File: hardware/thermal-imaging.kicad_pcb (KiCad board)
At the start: 2 copper layers, 40 x 40 mm, 39 parts, among them P1 CON-SENSOR, P2 Boot, Q1 Oscillator, U1 XMC1XXX24, U10 DRILL, U11 DRILL, U2 74LVC1G17, U3 74LVC1G17, U4 FLIR-Lepton, U5 AP7333-28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

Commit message: routing completed
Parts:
- added Fiducial_Mark: VAL**, kicad-libraries:Fiducial_Mark, F.Cu at (200.4, 114.9)
- added Fiducial_Mark: VAL**, kicad-libraries:Fiducial_Mark, F.Cu at (174.4, 118.9)
- added Fiducial_Mark: VAL**, kicad-libraries:Fiducial_Mark, F.Cu at (176.4, 84.9)
- added Fiducial_Mark: VAL**, kicad-libraries:Fiducial_Mark, F.Cu at (199.4, 82.9)
- added G***: Logo_31x31, kicad-libraries:Logo_31x31, F.Cu at (193.4, 114.6)
- added G***: LOGO, kicad-libraries:Logo_CoMCU, B.Cu at (186.4, 100.9)
- added G***: LOGO, kicad-libraries:WEEE_7mm, B.Cu at (194.4, 100.9)
- added VAL: CE_5mm, kicad-libraries:CE_5mm, B.Cu at (178.4, 100.9)
- moved FB1 2.80 mm to (196.2, 108.1)
- moved C1 1.60 mm to (198.4, 107.3), turned to 180 degrees
- moved C2 1.60 mm to (198.4, 108.9), turned to 180 degrees
- moved C12 1.41 mm to (172.3, 99.9)
- moved Q1 1.30 mm to (174.9, 99.9)
- moved R4 1.20 mm to (178.5, 98.6)
- moved C3 1.00 mm to (196.5, 82.4)
- moved U1 0.80 mm to (196.5, 86.3)
- moved RP1 0.22 mm to (200.9, 89.1)
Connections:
- U1 pad 16: (no net) -> RESET
- U1 pad 2: RESET -> (no net)
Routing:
- net 3V3: track 0.00 -> 116.1 mm, vias 0 -> 2
- net +2.8V: track 0.00 -> 96.9 mm, vias 0 -> 5
- net GND: track 0.00 -> 65.8 mm, vias 0 -> 42
- net RESET: track 0.00 -> 29.0 mm, vias 0 -> 6
- net SDA: track 0.00 -> 28.4 mm, vias 0 -> 6
- net VSYNC: track 0.00 -> 25.2 mm
- net SCL: track 0.00 -> 23.7 mm, vias 0 -> 4
- net M-MISO: track 0.00 -> 18.7 mm, vias 0 -> 2
- net +2.8V_INT: track 0.00 -> 16.9 mm, vias 0 -> 2
- net +1.2V_INT: track 0.00 -> 13.6 mm, vias 0 -> 2
- net Net-(RP3-Pad7): track 0.00 -> 10.4 mm
- net Net-(FILTER1-Pad1): track 0.00 -> 10.1 mm
- net Net-(C1-Pad2): track 0.00 -> 9.54 mm
- net Net-(FILTER1-Pad2): track 0.00 -> 8.47 mm
- net Net-(P2-Pad2): track 0.00 -> 8.39 mm
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- added copper zone on B.Cu, net GND
- added copper zone on F.Cu, net GND

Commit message: add description text
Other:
- board text added: "Copyright Tinkerforge GmbH 2017. This documentation describes Open Hardware and is licensed under the CERN OHL v. 1.1. You may redistribute and modify this documentation under the terms of the CERN OHL v.1.1. (http://ohwr.org/cernohl). This documentation is distributed WITHOUT ANY EXPRESS OR IMPLIED WARRANTY, INCLUDING OF MERCHANTABILITY, SATISFACTORY QUALITY AND FITNESS FOR A PARTICULAR PURPOSE.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"
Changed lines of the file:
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@@
     (links 151)
     (no_connects 0)
-    (area 166.324999 80.824999 206.475001 120.975001)
+    (area 165.544999 80.044999 207.255001 121.755001)
     (thickness 1.6)
-    (drawings 11)
+    (drawings 12)
     (tracks 522)
     (zones 0)
@@
   )
   (page A4)
+  (title_block
+    (title "Thermal Imaging Bricklet")
+    (date 2017-02-08)
+    (rev 1.0)
+    (company "Tinkerforge GmbH")
+    (comment 1 "Licensed under CERN OHL v.1.1")
+    (comment 2 "Copyright (©) 2017, B.Nordmeyer <bastian@tinkerforge.com>")
+  )
   (layers
     (0 F.Cu signal hide)
@@
   )
   (setup
-    (last_trace_width 0.3)
+    (last_trace_width 0.2)
     (user_trace_width 0.2)
     (user_trace_width 0.25)
@@
       (xy 2.48217 3.513666) (xy 2.482863 3.409859) (xy 2.482863 3.409859)) (layer B.SilkS) (width 0.1))
   )
+  (gr_text "Copyright Tinkerforge GmbH 2017.\nThis documentation describes Open Hardware and is licensed under the\nCERN OHL v. 1.1.\nYou may redistribute and modify this documentation under the terms of the\nCERN OHL v.1.1. (http://ohwr.org/cernohl). This documentation is distributed\nWITHOUT ANY EXPRESS OR IMPLIED WARRANTY, INCLUDING OF\nMERCHANTABILITY, SATISFACTORY QUALITY AND FITNESS FOR A\nPARTICULAR PURPOSE. Please see the CERN OHL v.1.1 for applicable\nconditions" (at 258.4 154.9) (layer Cmts.User)
+    (effects (font (size 0.8 0.8) (thickness 0.2)))
+  )
   (gr_text Status (at 186.4 82.6) (layer F.SilkS)

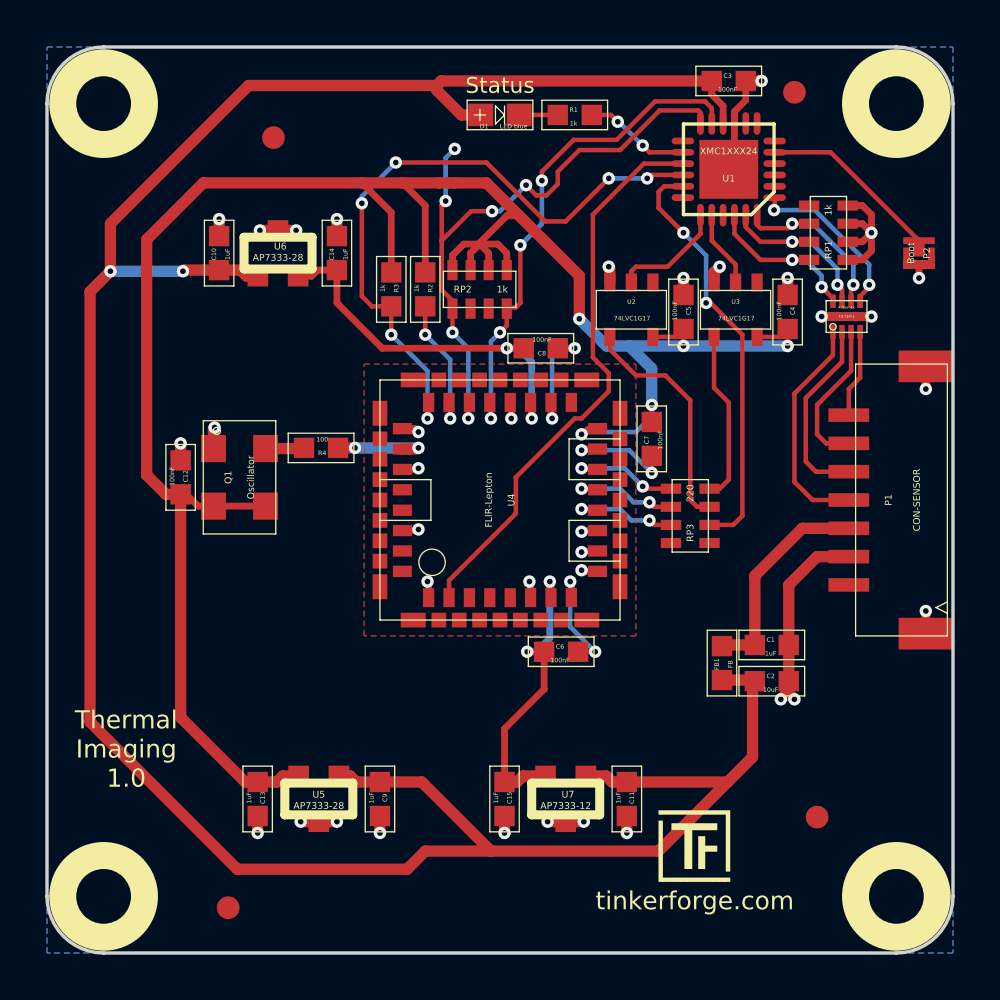
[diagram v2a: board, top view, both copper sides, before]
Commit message: fix wrong footprint
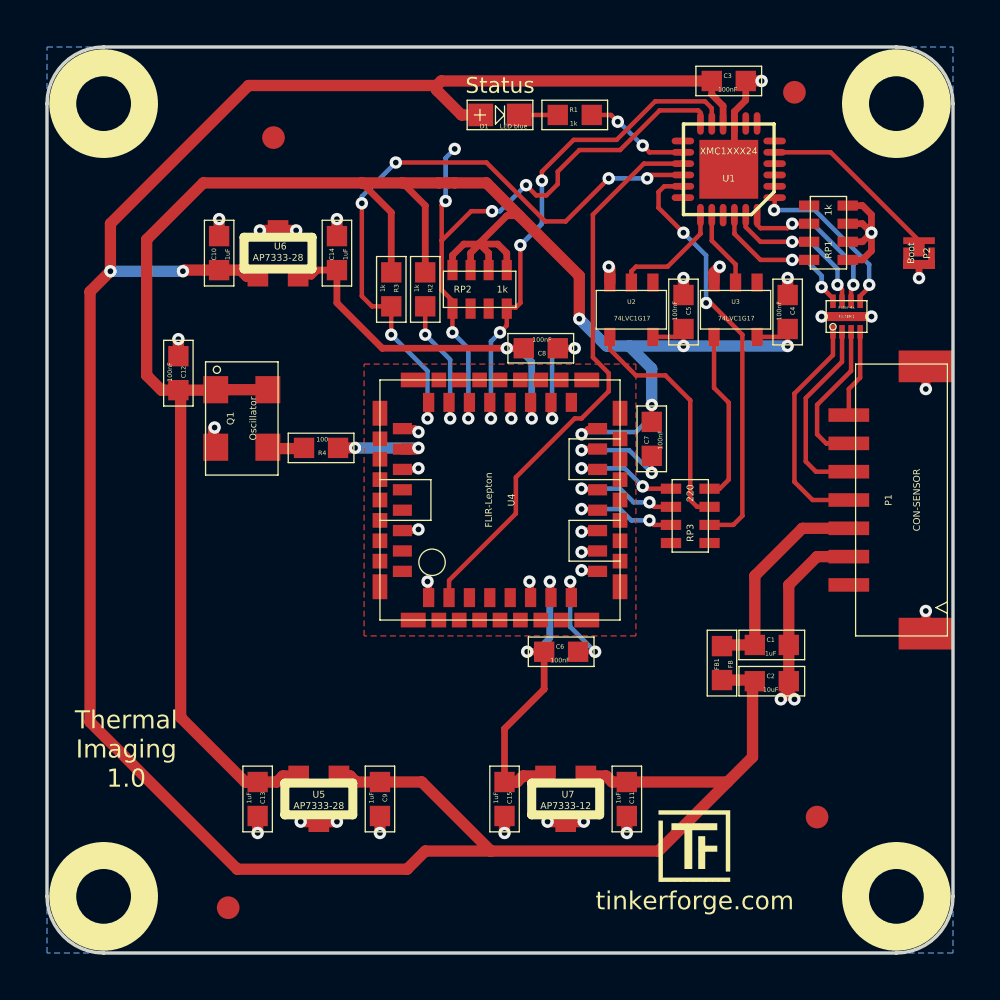
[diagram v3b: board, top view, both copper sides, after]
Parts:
- Q1: footprint CRYSTAL_5032 -> kicad-libraries:CRYSTAL_5032
- moved C12 4.60 mm to (172.2, 95.3)
- moved Q1 2.60 mm to (175.0, 97.3)
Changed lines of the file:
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@@
     (links 151)
     (no_connects 0)
-    (area 165.544999 80.044999 207.255001 121.755001)
+    (area 165.544999 80.044999 282.44286 160.84)
     (thickness 1.6)
     (drawings 12)
@@
   )
   (layers
-    (0 F.Cu signal hide)
+    (0 F.Cu signal)
     (31 B.Cu signal hide)
     (32 B.Adhes user hide)
@@
   )
   (setup
-    (last_trace_width 0.2)
+    (last_trace_width 0.5)
     (user_trace_width 0.2)
     (user_trace_width 0.25)
@@
   )
   (module kicad-libraries:0603F (layer F.Cu)
-    (at 172.3 99.9 90)
+    (at 172.2 95.3 90)
     (attr smd)
     (fp_text reference C12 (at 0.05 0.225 90) (layer F.SilkS)
@@
       (net 1 GND))
   )
-  (module CRYSTAL_5032 (layer F.Cu)
-    (at 174.9 99.9 270)
-    (fp_text reference Q1 (at 0 0.5 270) (layer F.SilkS)
-      (effects (font (size 0.3 0.3) (thickness 0.075)))
-    )
-    (fp_text value Oscillator (at 0 -0.5 270) (layer F.SilkS)
-      (effects (font (size 0.3 0.3) (thickness 0.075)))
-    )
-    (fp_circle (center -2.05 1) (end -2 1.15) (layer F.SilkS) (width 0.05))
-    (fp_line (start -2.5 -1.6) (end 2.5 -1.6) (layer F.SilkS) (width 0.05))
-    (fp_line (start 2.5 -1.6) (end 2.5 1.6) (layer F.SilkS) (width 0.05))
-    (fp_line (start 2.5 1.6) (end -2.5 1.6) (layer F.SilkS) (width 0.05))
-    (fp_line (start -2.5 1.6) (end -2.5 -1.6) (layer F.SilkS) (width 0.05))
-    (pad 1 smd rect (at 1.27 1.15 270) (size 1.2 1.1) (layers F.Cu F.Paste F.Mask)
-      (net 31 +2.8V))
-    (pad 2 smd rect (at -1.27 1.15 270) (size 1.2 1.1) (layers F.Cu F.Paste F.Mask)
-      (net 1 GND))
-    (pad 3 smd rect (at -1.27 -1.15 270) (size 1.2 1.1) (layers F.Cu F.Paste F.Mask)
-      (net 19 "Net-(Q1-Pad3)"))
-    (pad 4 smd rect (at 1.27 -1.15 270) (size 1.2 1.1) (layers F.Cu F.Paste F.Mask)
-      (net 31 +2.8V))
-  )
   (module 0603F (layer F.Cu)
     (at 189.7 83.9 180)
@@
       (xy 2.48217 3.513666) (xy 2.482863 3.409859) (xy 2.482863 3.409859)) (layer B.SilkS) (width 0.1))
   )
+  (module kicad-libraries:CRYSTAL_5032 (layer F.Cu)
+    (at 175 97.3 270)
+    (fp_text reference Q1 (at 0 0.5 270) (layer F.SilkS)
+      (effects (font (size 0.3 0.3) (thickness 0.075)))
+    )
+    (fp_text value Oscillator (at 0 -0.5 270) (layer F.SilkS)
+      (effects (font (size 0.3 0.3) (thickness 0.075)))
+    )
+    (fp_circle (center -2.15 1.1) (end -2.1 1.25) (layer F.SilkS) (width 0.05))
+    (fp_line (start -2.5 -1.6) (end 2.5 -1.6) (layer F.SilkS) (width 0.05))
+    (fp_line (start 2.5 -1.6) (end 2.5 1.6) (layer F.SilkS) (width 0.05))
+    (fp_line (start 2.5 1.6) (end -2.5 1.6) (layer F.SilkS) (width 0.05))
+    (fp_line (start -2.5 1.6) (end -2.5 -1.6) (layer F.SilkS) (width 0.05))
+    (pad 2 smd rect (at 1.27 1.15 270) (size 1.2 1.1) (layers F.Cu F.Paste F.Mask)
+      (net 1 GND))
+    (pad 1 smd rect (at -1.27 1.15 270) (size 1.2 1.1) (layers F.Cu F.Paste F.Mask)
+      (net 31 +2.8V))
+    (pad 4 smd rect (at -1.27 -1.15 270) (size 1.2 1.1) (layers F.Cu F.Paste F.Mask)
+      (net 31 +2.8V))
+    (pad 3 smd rect (at 1.27 -1.15 270) (size 1.2 1.1) (layers F.Cu F.Paste F.Mask)
+      (net 19 "Net-(Q1-Pad3)"))
+  )
   (gr_text "Copyright Tinkerforge GmbH 2017.\nThis documentation describes Open Hardware and is licensed under the\nCERN OHL v. 1.1.\nYou may redistribute and modify this documentation under the terms of the\nCERN OHL v.1.1. (http://ohwr.org/cernohl). This documentation is distributed\nWITHOUT ANY EXPRESS OR IMPLIED WARRANTY, INCLUDING OF\nMERCHANTABILITY, SATISFACTORY QUALITY AND FITNESS FOR A\nPARTICULAR PURPOSE. Please see the CERN OHL v.1.1 for applicable\nconditions" (at 258.4 154.9) (layer Cmts.User)
     (effects (font (size 0.8 0.8) (thickness 0.2)))
@@
     (effects (font (size 0.8 0.8) (thickness 0.15)))
   )
+  (segment (start 172.2 94.55) (end 172.2 93.8) (width 0.5) (layer F.Cu) (net 1))
+  (via (at 172.2 93.8) (size 0.55) (drill 0.25) (layers F.Cu B.Cu) (net 1))
   (segment (start 205.45 90.225) (end 205.45 90.4) (width 0.2) (layer F.Cu) (net 1))
   (segment (start 205.45 90.4) (end 205.35 90.5) (width 0.2) (layer F.Cu) (net 1))
@@
   (segment (start 197.25 82.4) (end 197.95 82.4) (width 0.5) (layer F.Cu) (net 1))
   (via (at 197.95 82.4) (size 0.55) (drill 0.25) (layers F.Cu B.Cu) (net 1))
-  (segment (start 172.3 99.15) (end 172.3 98.4) (width 0.5) (layer F.Cu) (net 1))
-  (via (at 172.3 98.4) (size 0.55) (drill 0.25) (layers F.Cu B.Cu) (net 1))
-  (segment (start 173.75 98.63) (end 173.75 97.75) (width 0.5) (layer F.Cu) (net 1))
-  (via (at 173.8 97.7) (size 0.55) (drill 0.25) (layers F.Cu B.Cu) (net 1))
-  (segment (start 173.75 97.75) (end 173.8 97.7) (width 0.5) (layer F.Cu) (net 1))
   (segment (start 190.71 102.25) (end 190.05 102.25) (width 0.3) (layer F.Cu) (net 1))
   (via (at 190 102.3) (size 0.55) (drill 0.25) (layers F.Cu B.Cu) (net 1))
@@
   (via (at 190 98.7) (size 0.55) (drill 0.25) (layers F.Cu B.Cu) (net 1))
   (segment (start 190.05 98.65) (end 190 98.7) (width 0.2) (layer F.Cu) (net 1))
+  (segment (start 173.75 98.63) (end 173.75 97.75) (width 0.5) (layer F.Cu) (net 1))
+  (via (at 173.8 97.7) (size 0.55) (drill 0.25) (layers F.Cu B.Cu) (net 1))
+  (segment (start 173.75 97.75) (end 173.8 97.7) (width 0.5) (layer F.Cu) (net 1))
   (segment (start 191.2 86.7) (end 189.3 88.6) (width 0.2) (layer F.Cu) (net 2))
   (segment (start 185.8 86) (end 181.8 86) (width 0.2) (layer F.Cu) (net 2))
@@
   (segment (start 184.15 104.45) (end 184.15 105.21) (width 0.2) (layer F.Cu) (net 30))
   (segment (start 192.75 86.05) (end 190.5 88.3) (width 0.2) (layer F.Cu) (net 30))
+  (segment (start 173.85 96.03) (end 176.15 96.03) (width 0.5) (layer F.Cu) (net 31))
+  (segment (start 172.2 96.05) (end 173.83 96.05) (width 0.5) (layer F.Cu) (net 31))
+  (segment (start 173.83 96.05) (end 173.85 96.03) (width 0.5) (layer F.Cu) (net 31))
+  (segment (start 172.2 96.05) (end 171.45 96.05) (width 0.5) (layer F.Cu) (net 31))
+  (segment (start 170.8 89.4) (end 173.3 86.9) (width 0.5) (layer F.Cu) (net 31))
+  (segment (start 173.3 86.9) (end 180.3 86.9) (width 0.5) (layer F.Cu) (net 31))
+  (segment (start 170.8 95.4) (end 170.8 89.4) (width 0.5) (layer F.Cu) (net 31))
+  (segment (start 171.45 96.05) (end 170.8 95.4) (width 0.5) (layer F.Cu) (net 31))
+  (segment (start 172.3 96.15) (end 172.3 110.5) (width 0.5) (layer F.Cu) (net 31))
+  (segment (start 175.15 113.35) (end 172.3 110.5) (width 0.5) (layer F.Cu) (net 31))
+  (segment (start 175.15 113.35) (end 175.7 113.35) (width 0.5) (layer F.Cu) (net 31))
+  (segment (start 172.3 96.15) (end 172.2 96.05) (width 0.5) (layer F.Cu) (net 31))
   (segment (start 185.5 89.55) (end 186.7 88.35) (width 0.3) (layer F.Cu) (net 31))
   (segment (start 186.7 88.35) (end 187.25 88.35) (width 0.3) (layer F.Cu) (net 31))
   (segment (start 185.5 89.6) (end 185.5 89.55) (width 0.3) (layer F.Cu) (net 31))
-  (segment (start 173.75 101.17) (end 176.05 101.17) (width 0.3) (layer F.Cu) (net 31))
-  (segment (start 172.3 100.65) (end 172.55 100.65) (width 0.3) (layer F.Cu) (net 31))
-  (segment (start 172.55 100.65) (end 173.07 101.17) (width 0.3) (layer F.Cu) (net 31))
-  (segment (start 173.07 101.17) (end 173.75 101.17) (width 0.3) (layer F.Cu) (net 31))
   (segment (start 193.1 96.7) (end 193.1 95.1) (width 0.5) (layer B.Cu) (net 31))
   (segment (start 193.1 95.1) (end 192.1 94.1) (width 0.5) (layer B.Cu) (net 31))
@@
   (via (at 199.1 94.1) (size 0.55) (drill 0.25) (layers F.Cu B.Cu) (net 31))
   (segment (start 199.1 94.1) (end 199.1 93.35) (width 0.2) (layer F.Cu) (net 31))
-  (segment (start 172.3 100.65) (end 171.65 100.65) (width 0.5) (layer F.Cu) (net 31))
   (via (at 194.5 94.1) (size 0.55) (drill 0.25) (layers F.Cu B.Cu) (net 31))
   (segment (start 194.5 94.1) (end 194.5 93.35) (width 0.2) (layer F.Cu) (net 31))
@@
   (segment (start 182.1 86.9) (end 183.7 86.9) (width 0.5) (layer F.Cu) (net 31))
   (segment (start 192.1 94.1) (end 194.5 94.1) (width 0.5) (layer B.Cu) (net 31))
-  (segment (start 173.3 86.9) (end 180.3 86.9) (width 0.5) (layer F.Cu) (net 31))
   (segment (start 180.3 86.9) (end 182.1 86.9) (width 0.5) (layer F.Cu) (net 31))
-  (segment (start 170.8 89.4) (end 173.3 86.9) (width 0.5) (layer F.Cu) (net 31))
-  (segment (start 170.8 99.8) (end 170.8 89.4) (width 0.5) (layer F.Cu) (net 31))
-  (segment (start 171.65 100.65) (end 170.8 99.8) (width 0.5) (layer F.Cu) (net 31))
-  (segment (start 175.7 113.35) (end 175.15 113.35) (width 0.5) (layer F.Cu) (net 31))
-  (segment (start 172.3 110.5) (end 172.3 100.65) (width 0.5) (layer F.Cu) (net 31))
-  (segment (start 175.15 113.35) (end 172.3 110.5) (width 0.5) (layer F.Cu) (net 31))
   (segment (start 177.511 113.084) (end 176.816 113.084) (width 0.5) (layer F.Cu) (net 31))
-  (segment (start 176.55 113.35) (end 175.7 113.35) (width 0.5) (layer F.Cu) (net 31))
   (segment (start 176.816 113.084) (end 176.55 113.35) (width 0.5) (layer F.Cu) (net 31))
+  (segment (start 176.55 113.35) (end 175.7 113.35) (width 0.5) (layer F.Cu) (net 31))
   (segment (start 190.71 97.75) (end 190.25 97.75) (width 0.2) (layer F.Cu) (net 31))
   (segment (start 193.1 96.7) (end 193.1 97.45) (width 0.2) (layer F.Cu) (net 31))

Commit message: fix text orientation
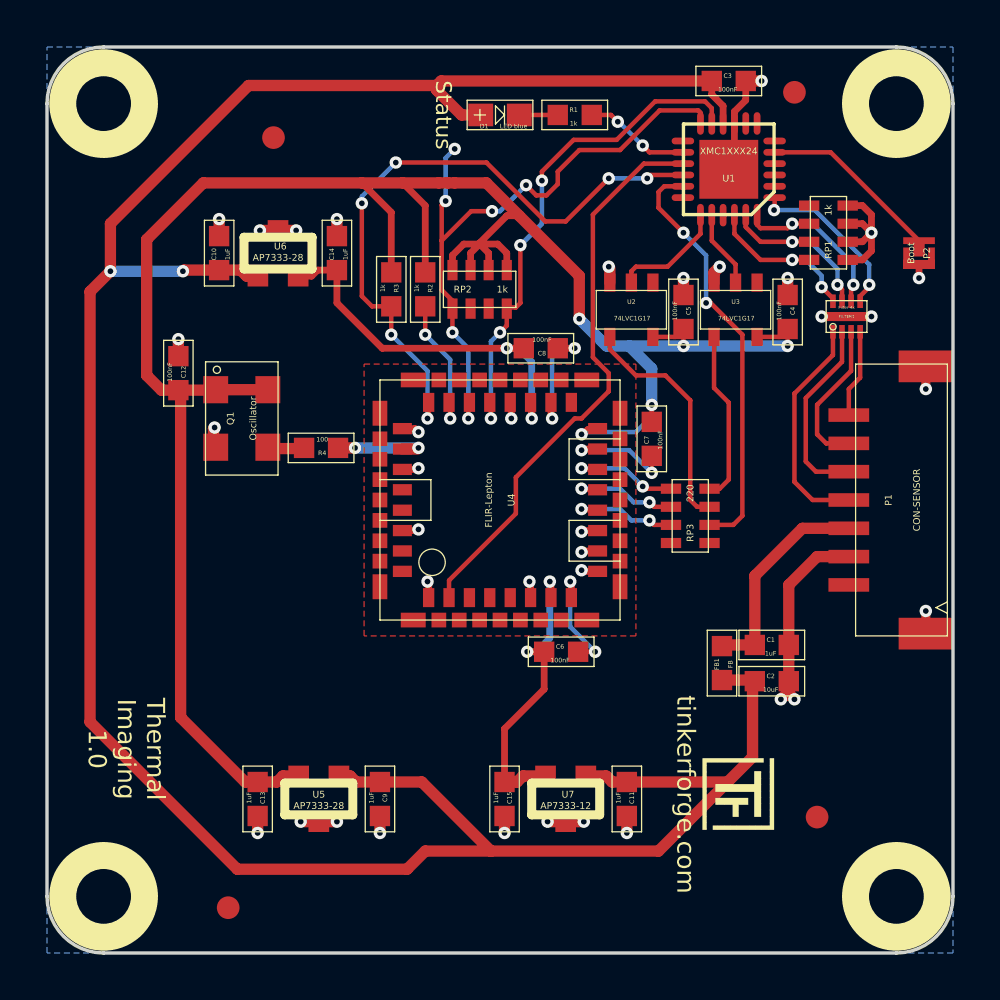
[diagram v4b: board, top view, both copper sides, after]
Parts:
- moved G*** 5.59 mm to (198.5, 112.3), turned to 270 degrees
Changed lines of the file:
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@@
   )
   (setup
-    (last_trace_width 0.5)
+    (last_trace_width 0.2)
     (user_trace_width 0.2)
     (user_trace_width 0.25)
@@
   )
   (module kicad-libraries:Logo_31x31 (layer F.Cu)
-    (at 193.4 114.6)
-    (fp_text reference G*** (at 1.34874 2.97434) (layer F.SilkS) hide
+    (at 198.5 112.3 270)
+    (fp_text reference G*** (at 1.34874 2.97434 270) (layer F.SilkS) hide
       (effects (font (size 0.29972 0.29972) (thickness 0.0762)))
     )
-    (fp_text value Logo_31x31 (at 1.651 0.59944) (layer F.SilkS) hide
+    (fp_text value Logo_31x31 (at 1.651 0.59944 270) (layer F.SilkS) hide
       (effects (font (size 0.29972 0.29972) (thickness 0.0762)))
     )
@@
     (effects (font (size 0.8 0.8) (thickness 0.2)))
   )
-  (gr_text Status (at 186.4 82.6) (layer F.SilkS)
+  (gr_text Status (at 183.9 83.9 270) (layer F.SilkS)
     (effects (font (size 0.7 0.7) (thickness 0.15)))
   )
@@
   (gr_arc (start 203.9 118.4) (end 206.4 118.4) (angle 90) (layer Edge.Cuts) (width 0.15))
   (gr_arc (start 168.9 118.4) (end 168.9 120.9) (angle 90) (layer Edge.Cuts) (width 0.15))
-  (gr_text "Thermal\nImaging\n1.0" (at 169.9 111.9) (layer F.SilkS)
+  (gr_text "Thermal\nImaging\n1.0" (at 169.9 111.9 270) (layer F.SilkS)
     (effects (font (size 0.8 0.8) (thickness 0.15)))
   )
-  (gr_text tinkerforge.com (at 195 118.6) (layer F.SilkS)
+  (gr_text tinkerforge.com (at 194.6 113.9 270) (layer F.SilkS)
     (effects (font (size 0.8 0.8) (thickness 0.15)))
   )

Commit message: change text orientation
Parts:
- moved G*** 6.39 mm to (193.6, 116.4), turned to 90 degrees
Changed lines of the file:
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@@
   )
   (module kicad-libraries:Logo_31x31 (layer F.Cu)
-    (at 198.5 112.3 270)
-    (fp_text reference G*** (at 1.34874 2.97434 270) (layer F.SilkS) hide
+    (at 193.6 116.4 90)
+    (fp_text reference G*** (at 1.34874 2.97434 90) (layer F.SilkS) hide
       (effects (font (size 0.29972 0.29972) (thickness 0.0762)))
     )
-    (fp_text value Logo_31x31 (at 1.651 0.59944 270) (layer F.SilkS) hide
+    (fp_text value Logo_31x31 (at 1.651 0.59944 90) (layer F.SilkS) hide
       (effects (font (size 0.29972 0.29972) (thickness 0.0762)))
     )
@@
     (effects (font (size 0.8 0.8) (thickness 0.2)))
   )
-  (gr_text Status (at 183.9 83.9 270) (layer F.SilkS)
+  (gr_text Status (at 184.3 83.3 90) (layer F.SilkS)
     (effects (font (size 0.7 0.7) (thickness 0.15)))
   )
@@
   (gr_arc (start 203.9 118.4) (end 206.4 118.4) (angle 90) (layer Edge.Cuts) (width 0.15))
   (gr_arc (start 168.9 118.4) (end 168.9 120.9) (angle 90) (layer Edge.Cuts) (width 0.15))
-  (gr_text "Thermal\nImaging\n1.0" (at 169.9 111.9 270) (layer F.SilkS)
+  (gr_text "Thermal\nImaging\n1.0" (at 169.9 111.9 90) (layer F.SilkS)
     (effects (font (size 0.8 0.8) (thickness 0.15)))
   )
-  (gr_text tinkerforge.com (at 194.6 113.9 270) (layer F.SilkS)
+  (gr_text tinkerforge.com (at 197.7 114.8 90) (layer F.SilkS)
     (effects (font (size 0.8 0.8) (thickness 0.15)))
   )
